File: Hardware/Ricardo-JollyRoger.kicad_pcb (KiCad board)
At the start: 4 copper layers, 45.8 x 35.8 mm, 88 parts, among them J1 RBUS, J2 USB_C_Receptacle_USB2.0, J3 Conn_01x08_Pin, J4 Conn_01x06_Pin, U1 ESP32-S3, U2 SN65HVD230, U3 LM66200DRLR, U4 MAX77827AEFD+T, U5 SC4215ASTRT, U7 LM66200DRLR, U8 ZDSD04GLGEAG, Y1 R940000171

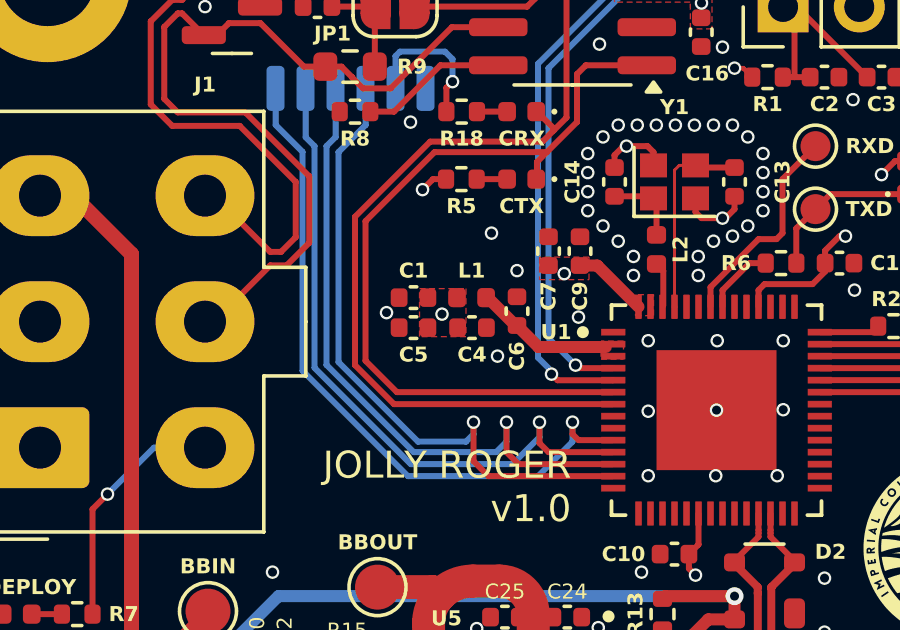
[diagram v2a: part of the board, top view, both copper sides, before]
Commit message: Updated capacitor layout
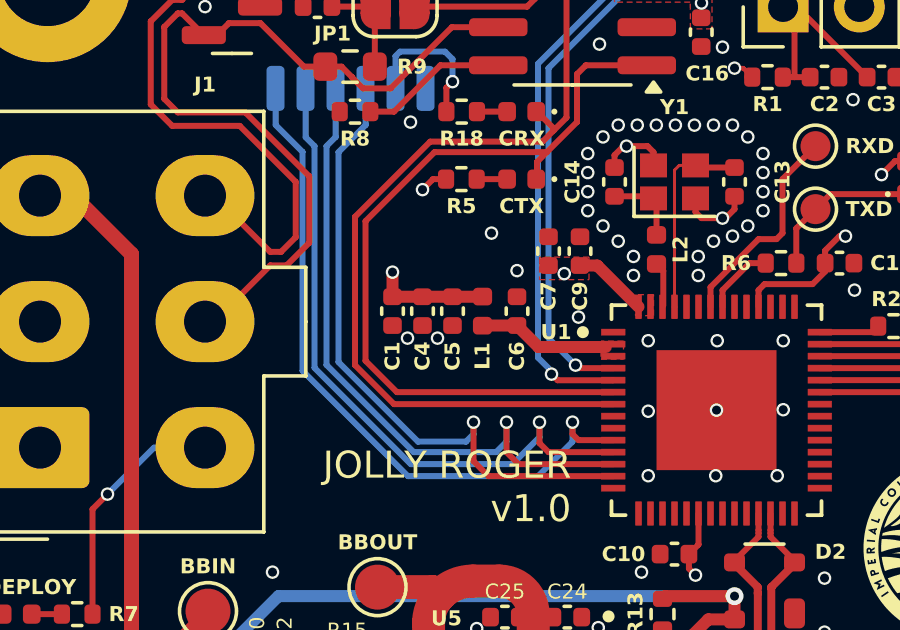
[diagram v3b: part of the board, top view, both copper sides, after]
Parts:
- moved C4 1.74 mm to (94.9, 59.5), turned to -90 degrees
- moved C5 1.41 mm to (95.9, 59.5), turned to -90 degrees
- moved C1 0.83 mm to (93.9, 59.5), turned to -90 degrees
- moved L1 0.58 mm to (96.9, 59.5), turned to -90 degrees
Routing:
- net +3V3: track 28.0 -> 31.8 mm

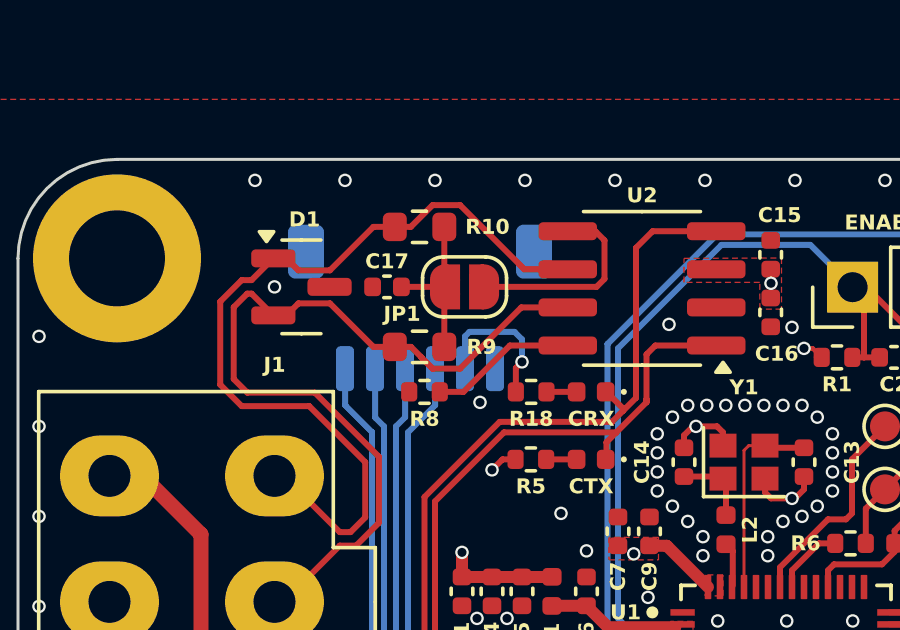
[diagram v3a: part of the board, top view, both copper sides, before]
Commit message: Changed GPIO breakout to 8 pin connector
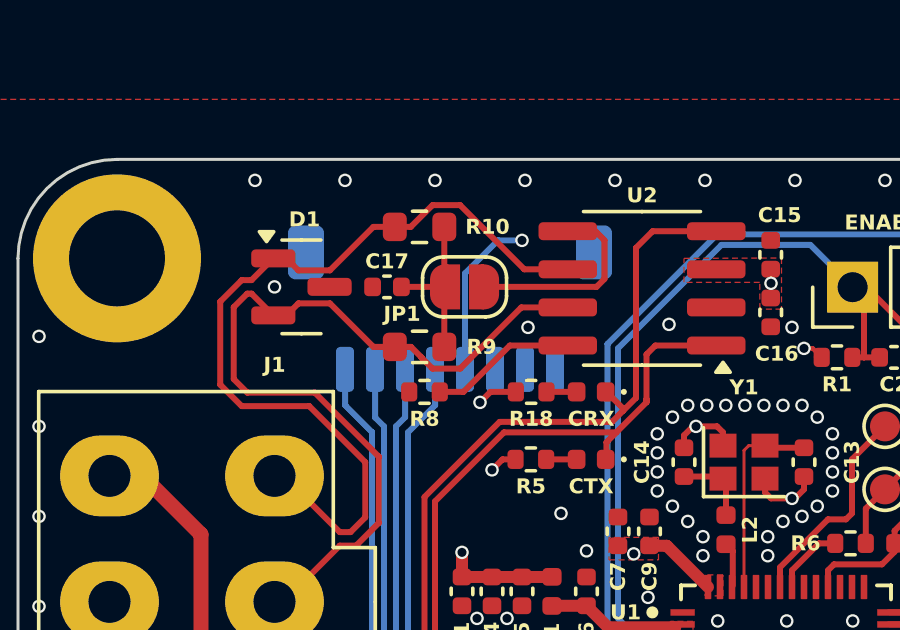
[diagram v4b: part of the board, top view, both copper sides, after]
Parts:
- J4: value Conn_01x06_Pin -> Conn_01x08_Pin; footprint Connector_Molex:Molex_Pico-Clasp_202396-0607_1x06-1MP_P1.00mm_Horizontal -> Connector_Molex:Molex_Pico-Clasp_202396-0807_1x08-1MP_P1.00mm_Horizontal
- moved J4 1.00 mm to (93.5, 50.1)
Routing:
- net +3V3: track 31.8 -> 33.7 mm, vias 15 -> 16

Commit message: Incorporated review feedback
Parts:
- moved C2 2.02 mm to (110.3, 51.7)
- moved R1 2.00 mm to (108.4, 51.7)
- moved R3 1.49 mm to (114.1, 52.7)
- moved C7 1.02 mm to (99.1, 58.5)
- moved C9 1.02 mm to (100.1, 58.5)
- moved C3 1.01 mm to (110.3, 52.7)
- moved C8 0.98 mm to (114.1, 51.7), turned to 0 degrees
- moved R20 0.51 mm to (110.1, 60.0)
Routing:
- net +3V3: track 33.7 -> 40.7 mm
- net Net-(U1-GPIO37): track 2.03 -> 1.51 mm
- net GND: vias 109 -> 113
